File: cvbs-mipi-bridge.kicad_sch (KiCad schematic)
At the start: 114 parts, among them IC1 ADV7282-M, IC2 TLV70018, IC4 SN74AUP1G17DCKR, IC5 SN74AUP1G17DCKR, J1 WE_68715014522, J2 1053131102, J3 KLPX-0848A-2-Y, J4 KLPX-0848A-2-Y, J5 KLPX-0848A-2-Y, J6 KLPX-0848A-2-Y, J7 61300211121, Q1 BSS138APW, Q2 BSS138APW, Q3 BSS138APW, Q4 BSS138APW, Y1 ABM8G-28.63636MHZ-18-D2Y-T

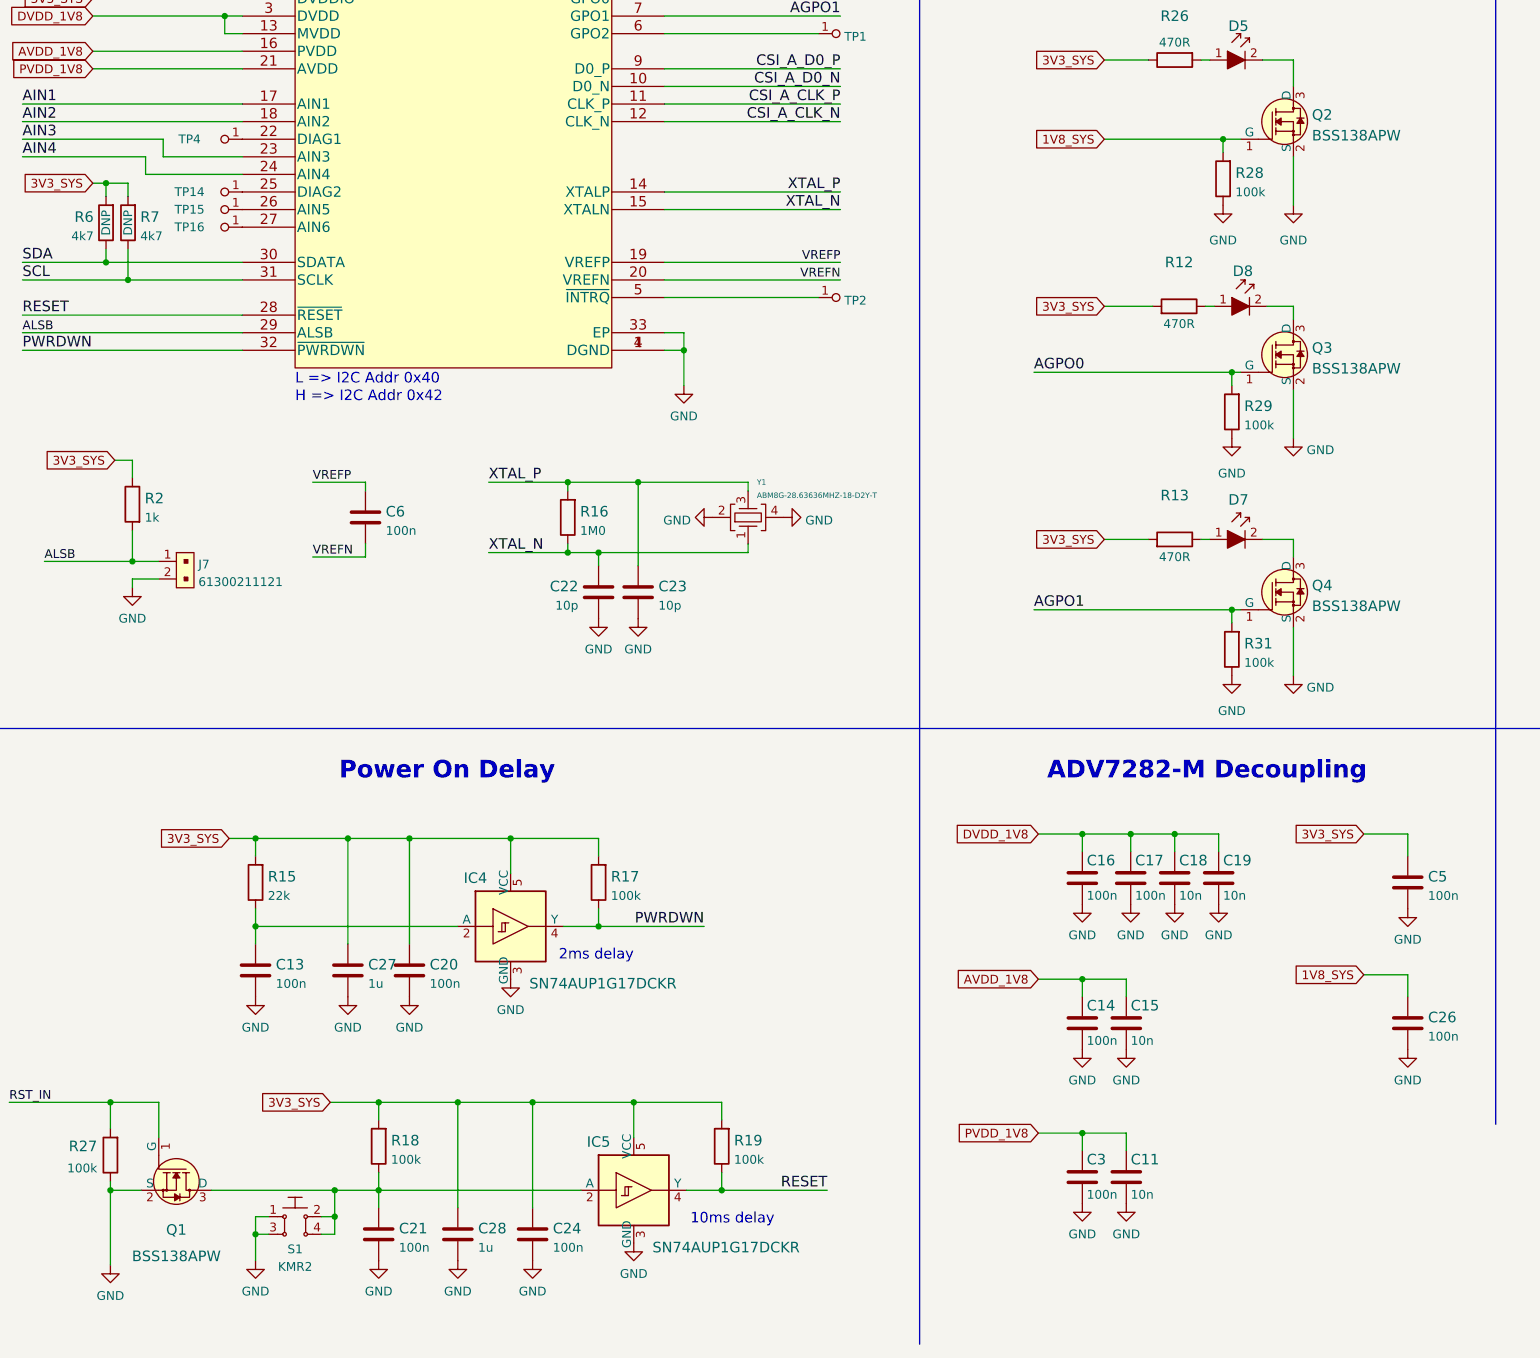
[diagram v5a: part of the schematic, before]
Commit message: Update Q1-Q4 from global library on SCH and PCB
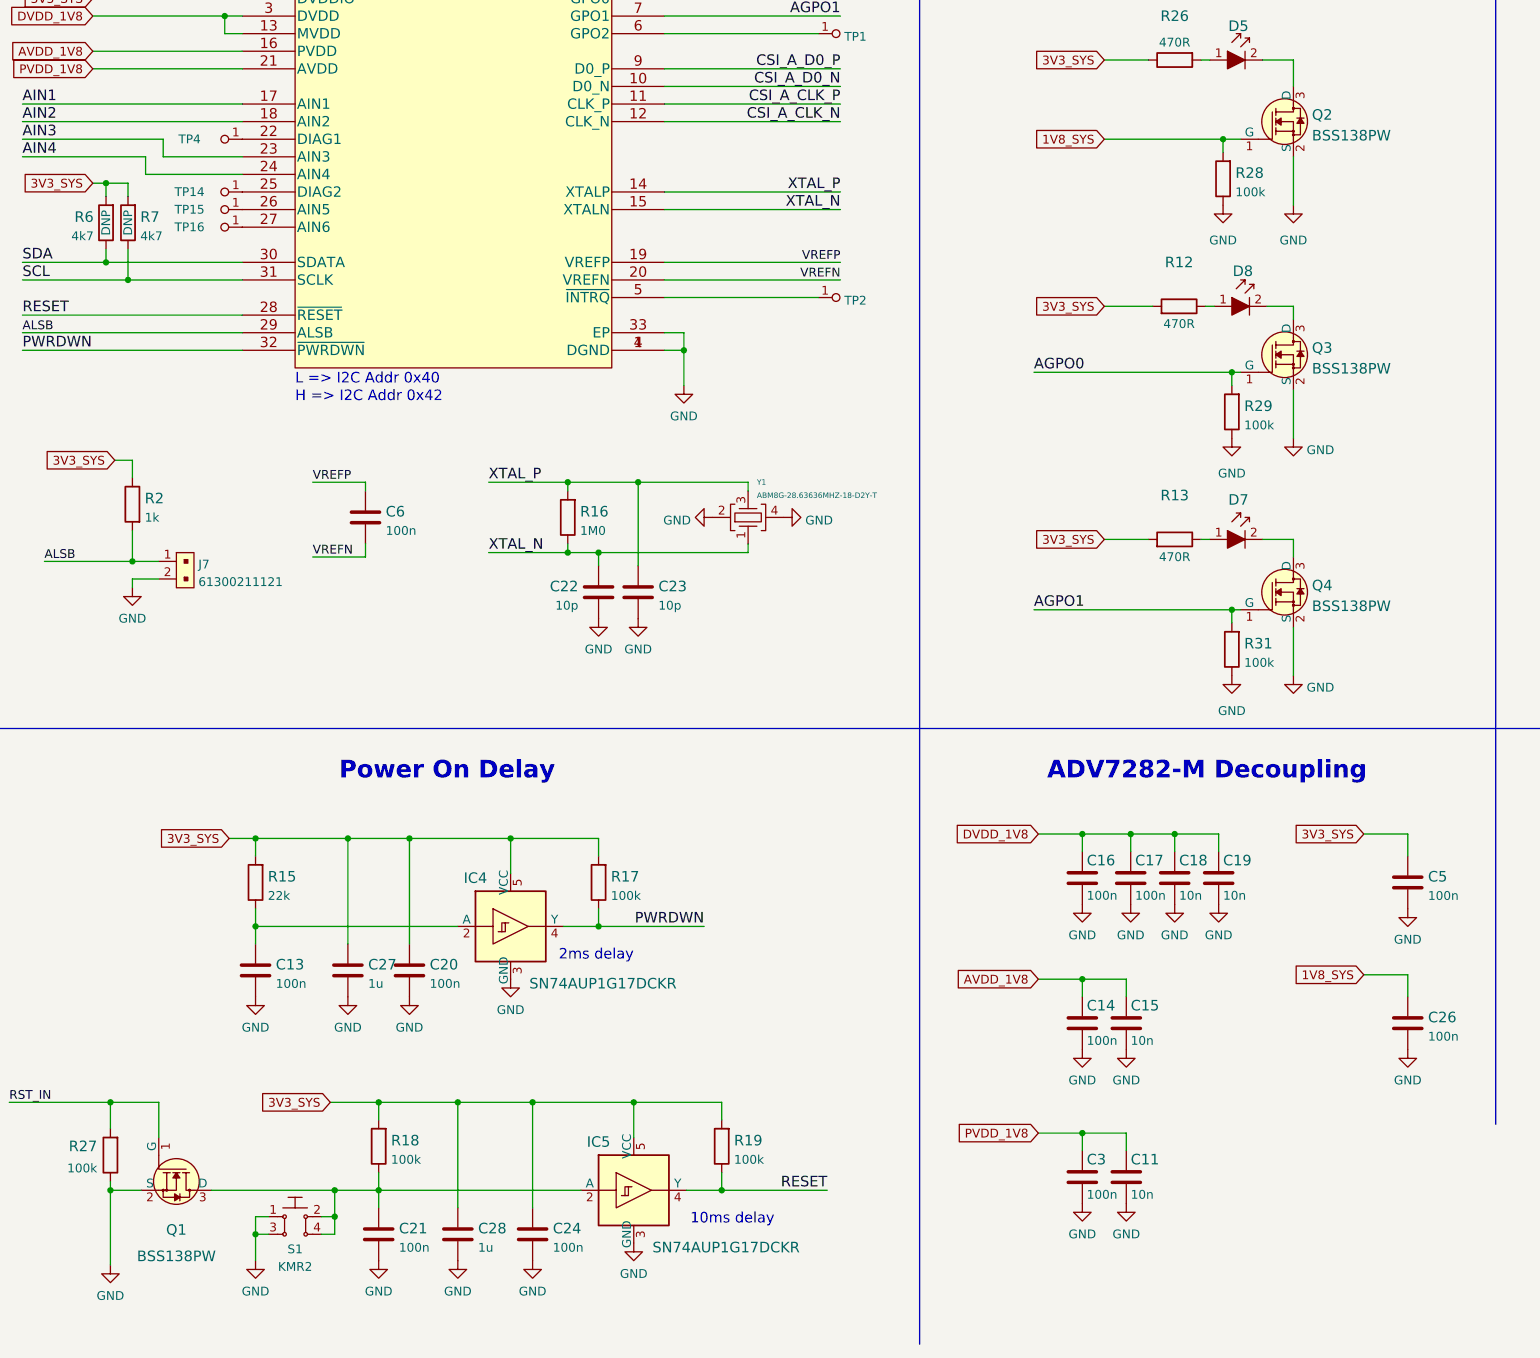
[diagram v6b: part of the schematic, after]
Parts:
- Q1, Q2, Q3, Q4: value BSS138APW -> BSS138PW; footprint cvbs-mipi-bridge-footprints:SC70-3 -> antmicro-footprints:SC70-3; symbol cvbs-mipi-bridge:BSS138APW -> antmicroTransistorsFETsMOSFETsSingle:BSS138PW; Manufacturer ON Semiconductor -> Nexperia
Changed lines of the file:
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@@
     (pin "4")
   )
-  (symbol (lib_id "cvbs-mipi-bridge:BSS138APW") (at 127 262.255 270) (unit 1)
+  (symbol (lib_id "antmicroTransistorsFETsMOSFETsSingle:BSS138PW") (at 127 262.255 270) (unit 1)
     (in_bom yes) (on_board yes) (fields_autoplaced)
     (property "Reference" "Q1" (id 0) (at 127 267.97 90)
       (effects (font (size 1.524 1.524)))
     )
-    (property "Value" "BSS138APW" (id 1) (at 127 271.78 90)
+    (property "Value" "BSS138PW" (id 1) (at 127 271.78 90)
       (effects (font (size 1.524 1.524)))
     )
-    (property "Footprint" "cvbs-mipi-bridge-footprints:SC70-3" (id 2) (at 132.08 267.335 0)
-      (effects (font (size 1.524 1.524)) (justify left) hide)
-    )
-    (property "Datasheet" "" (id 3) (at 134.62 267.335 0)
+    (property "Footprint" "antmicro-footprints:SC70-3" (id 2) (at 132.08 267.335 0)
+      (effects (font (size 1.524 1.524)) (justify left) hide)
+    )
+    (property "Datasheet" "https://assets.nexperia.com/documents/data-sheet/BSS138PW.pdf" (id 3) (at 134.62 267.335 0)
       (effects (font (size 1.524 1.524)) (justify left) hide)
     )
@@
       (effects (font (size 1.524 1.524)) (justify left) hide)
     )
-    (property "Manufacturer" "ON Semiconductor" (id 5) (at 154.94 267.335 0)
+    (property "Manufacturer" "Nexperia" (id 5) (at 154.94 267.335 0)
       (effects (font (size 1.524 1.524)) (justify left) hide)
     )
@@
     (pin "2")
   )
-  (symbol (lib_id "cvbs-mipi-bridge:BSS138APW") (at 288.29 175.895 0) (unit 1)
+  (symbol (lib_id "antmicroTransistorsFETsMOSFETsSingle:BSS138PW") (at 288.29 175.895 0) (unit 1)
     (in_bom yes) (on_board yes)
     (property "Reference" "Q4" (id 0) (at 290.957 174.9188 0)
       (effects (font (size 1.524 1.524)) (justify left))
     )
-    (property "Value" "BSS138APW" (id 1) (at 290.957 177.9122 0)
+    (property "Value" "BSS138PW" (id 1) (at 290.957 177.9122 0)
       (effects (font (size 1.524 1.524)) (justify left))
     )
-    (property "Footprint" "cvbs-mipi-bridge-footprints:SC70-3" (id 2) (at 293.37 170.815 0)
-      (effects (font (size 1.524 1.524)) (justify left) hide)
-    )
-    (property "Datasheet" "" (id 3) (at 293.37 168.275 0)
+    (property "Footprint" "antmicro-footprints:SC70-3" (id 2) (at 293.37 170.815 0)
+      (effects (font (size 1.524 1.524)) (justify left) hide)
+    )
+    (property "Datasheet" "https://assets.nexperia.com/documents/data-sheet/BSS138PW.pdf" (id 3) (at 293.37 168.275 0)
       (effects (font (size 1.524 1.524)) (justify left) hide)
     )
@@
       (effects (font (size 1.524 1.524)) (justify left) hide)
     )
-    (property "Manufacturer" "ON Semiconductor" (id 5) (at 293.37 147.955 0)
+    (property "Manufacturer" "Nexperia" (id 5) (at 293.37 147.955 0)
       (effects (font (size 1.524 1.524)) (justify left) hide)
     )
@@
     (pin "2")
   )
-  (symbol (lib_id "cvbs-mipi-bridge:BSS138APW") (at 288.29 107.95 0) (unit 1)
+  (symbol (lib_id "antmicroTransistorsFETsMOSFETsSingle:BSS138PW") (at 288.29 107.95 0) (unit 1)
     (in_bom yes) (on_board yes)
     (property "Reference" "Q2" (id 0) (at 290.957 106.9738 0)
       (effects (font (size 1.524 1.524)) (justify left))
     )
-    (property "Value" "BSS138APW" (id 1) (at 290.957 109.9672 0)
+    (property "Value" "BSS138PW" (id 1) (at 290.957 109.9672 0)
       (effects (font (size 1.524 1.524)) (justify left))
     )
-    (property "Footprint" "cvbs-mipi-bridge-footprints:SC70-3" (id 2) (at 293.37 102.87 0)
-      (effects (font (size 1.524 1.524)) (justify left) hide)
-    )
-    (property "Datasheet" "" (id 3) (at 293.37 100.33 0)
+    (property "Footprint" "antmicro-footprints:SC70-3" (id 2) (at 293.37 102.87 0)
+      (effects (font (size 1.524 1.524)) (justify left) hide)
+    )
+    (property "Datasheet" "https://assets.nexperia.com/documents/data-sheet/BSS138PW.pdf" (id 3) (at 293.37 100.33 0)
       (effects (font (size 1.524 1.524)) (justify left) hide)
     )
@@
       (effects (font (size 1.524 1.524)) (justify left) hide)
     )
-    (property "Manufacturer" "ON Semiconductor" (id 5) (at 293.37 80.01 0)
+    (property "Manufacturer" "Nexperia" (id 5) (at 293.37 80.01 0)
       (effects (font (size 1.524 1.524)) (justify left) hide)
     )
@@
     (pin "1")
   )
-  (symbol (lib_id "cvbs-mipi-bridge:BSS138APW") (at 288.29 141.605 0) (unit 1)
+  (symbol (lib_id "antmicroTransistorsFETsMOSFETsSingle:BSS138PW") (at 288.29 141.605 0) (unit 1)
     (in_bom yes) (on_board yes)
     (property "Reference" "Q3" (id 0) (at 290.957 140.6288 0)
       (effects (font (size 1.524 1.524)) (justify left))
     )
-    (property "Value" "BSS138APW" (id 1) (at 290.957 143.6222 0)
+    (property "Value" "BSS138PW" (id 1) (at 290.957 143.6222 0)
       (effects (font (size 1.524 1.524)) (justify left))
     )
-    (property "Footprint" "cvbs-mipi-bridge-footprints:SC70-3" (id 2) (at 293.37 136.525 0)
-      (effects (font (size 1.524 1.524)) (justify left) hide)
-    )
-    (property "Datasheet" "" (id 3) (at 293.37 133.985 0)
+    (property "Footprint" "antmicro-footprints:SC70-3" (id 2) (at 293.37 136.525 0)
+      (effects (font (size 1.524 1.524)) (justify left) hide)
+    )
+    (property "Datasheet" "https://assets.nexperia.com/documents/data-sheet/BSS138PW.pdf" (id 3) (at 293.37 133.985 0)
       (effects (font (size 1.524 1.524)) (justify left) hide)
     )
@@
       (effects (font (size 1.524 1.524)) (justify left) hide)
     )
-    (property "Manufacturer" "ON Semiconductor" (id 5) (at 293.37 113.665 0)
+    (property "Manufacturer" "Nexperia" (id 5) (at 293.37 113.665 0)
       (effects (font (size 1.524 1.524)) (justify left) hide)
     )
@@
     )
     (path "/95e1a59b-1a6c-467c-9037-83f08094ade6"
-      (reference "Q1") (unit 1) (value "BSS138APW") (footprint "cvbs-mipi-bridge-footprints:SC70-3")
+      (reference "Q1") (unit 1) (value "BSS138PW") (footprint "antmicro-footprints:SC70-3")
     )
     (path "/f68d1f32-2d93-4f69-b3c5-d0b861598112"
-      (reference "Q2") (unit 1) (value "BSS138APW") (footprint "cvbs-mipi-bridge-footprints:SC70-3")
+      (reference "Q2") (unit 1) (value "BSS138PW") (footprint "antmicro-footprints:SC70-3")
     )
     (path "/fac377af-49d7-4627-96ae-79376b872ab9"
-      (reference "Q3") (unit 1) (value "BSS138APW") (footprint "cvbs-mipi-bridge-footprints:SC70-3")
+      (reference "Q3") (unit 1) (value "BSS138PW") (footprint "antmicro-footprints:SC70-3")
     )
     (path "/aad57a2e-9eca-4168-bc4f-4b035b4e6956"
-      (reference "Q4") (unit 1) (value "BSS138APW") (footprint "cvbs-mipi-bridge-footprints:SC70-3")
+      (reference "Q4") (unit 1) (value "BSS138PW") (footprint "antmicro-footprints:SC70-3")
     )
     (path "/44b415ce-6f62-45ef-b8e2-efa97d049c0e"

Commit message: Increase revision number to 1.0.1 - update title blocks & PCB marking
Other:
- company: (none) -> Antmicro Ltd.
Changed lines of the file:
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@@
   (title_block
     (title "CVBS-MIPI Bridge")
-    (date "2022-09-29")
-    (rev "1.0.0")
+    (date "2022-11-04")
+    (rev "1.0.1")
+    (company "Antmicro Ltd.")
     (comment 1 "www.antmicro.com")
-    (comment 2 "Antmicro Ltd.")
   )
   (junction (at 69.088 115.57) (diameter 0) (color 0 0 0 0)

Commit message: SCH: Change selected Power On Delay elements' footprints to thermal-relief variants
Thermal reliefs added to: R27, C13, C20, C21, C24, C27, C28
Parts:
- C13, C20, C21, C24, C27, C28: footprint cvbs-mipi-bridge-footprints:0402-cap -> cvbs-mipi-bridge-footprints:0402-cap_ThermalReliefs_ZoneSizeSettings
- R27: footprint cvbs-mipi-bridge-footprints:0402-res -> cvbs-mipi-bridge-footprints:0402-res_ThermalReliefs_ZoneSizeSettings
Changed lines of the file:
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@@
       (effects (font (size 1.524 1.524)) hide)
     )
-    (property "Footprint" "cvbs-mipi-bridge-footprints:0402-cap" (id 2) (at 183.515 263.525 0)
+    (property "Footprint" "cvbs-mipi-bridge-footprints:0402-cap_ThermalReliefs_ZoneSizeSettings" (id 2) (at 183.515 263.525 0)
       (effects (font (size 1.524 1.524)) (justify left) hide)
     )
@@
       (effects (font (size 1.524 1.524)) hide)
     )
-    (property "Footprint" "cvbs-mipi-bridge-footprints:0402-cap" (id 2) (at 143.51 225.425 0)
+    (property "Footprint" "cvbs-mipi-bridge-footprints:0402-cap_ThermalReliefs_ZoneSizeSettings" (id 2) (at 143.51 225.425 0)
       (effects (font (size 1.524 1.524)) (justify left) hide)
     )
@@
       (effects (font (size 1.524 1.524)) hide)
     )
-    (property "Footprint" "cvbs-mipi-bridge-footprints:0402-cap" (id 2) (at 161.29 263.525 0)
+    (property "Footprint" "cvbs-mipi-bridge-footprints:0402-cap_ThermalReliefs_ZoneSizeSettings" (id 2) (at 161.29 263.525 0)
       (effects (font (size 1.524 1.524)) (justify left) hide)
     )
@@
       (effects (font (size 1.524 1.524)) hide)
     )
-    (property "Footprint" "cvbs-mipi-bridge-footprints:0402-cap" (id 2) (at 172.72 263.525 0)
+    (property "Footprint" "cvbs-mipi-bridge-footprints:0402-cap_ThermalReliefs_ZoneSizeSettings" (id 2) (at 172.72 263.525 0)
       (effects (font (size 1.524 1.524)) (justify left) hide)
     )
@@
       (effects (font (size 1.524 1.524)) hide)
     )
-    (property "Footprint" "cvbs-mipi-bridge-footprints:0402-cap" (id 2) (at 156.845 225.425 0)
+    (property "Footprint" "cvbs-mipi-bridge-footprints:0402-cap_ThermalReliefs_ZoneSizeSettings" (id 2) (at 156.845 225.425 0)
       (effects (font (size 1.524 1.524)) (justify left) hide)
     )
@@
       (effects (font (size 1.524 1.524)) hide)
     )
-    (property "Footprint" "cvbs-mipi-bridge-footprints:0402-cap" (id 2) (at 165.735 225.425 0)
+    (property "Footprint" "cvbs-mipi-bridge-footprints:0402-cap_ThermalReliefs_ZoneSizeSettings" (id 2) (at 165.735 225.425 0)
       (effects (font (size 1.524 1.524)) (justify left) hide)
     )
@@
       (effects (font (size 1.524 1.524)) hide)
     )
-    (property "Footprint" "cvbs-mipi-bridge-footprints:0402-res" (id 2) (at 112.395 252.095 0)
+    (property "Footprint" "cvbs-mipi-bridge-footprints:0402-res_ThermalReliefs_ZoneSizeSettings" (id 2) (at 112.395 252.095 0)
       (effects (font (size 1.524 1.524)) (justify left) hide)
     )
@@
     )
     (path "/1bee2d5b-6bc8-4cce-a6e3-1f3bf9745bb9"
-      (reference "C13") (unit 1) (value "C_100n_0402") (footprint "cvbs-mipi-bridge-footprints:0402-cap")
+      (reference "C13") (unit 1) (value "C_100n_0402") (footprint "cvbs-mipi-bridge-footprints:0402-cap_ThermalReliefs_ZoneSizeSettings")
     )
     (path "/a6cf3c89-c358-4fe5-8c48-55a885e26635"
@@
     )
     (path "/d9a4ccc3-9031-42be-9255-f7e52bdbb0e2"
-      (reference "C20") (unit 1) (value "C_100n_0402") (footprint "cvbs-mipi-bridge-footprints:0402-cap")
+      (reference "C20") (unit 1) (value "C_100n_0402") (footprint "cvbs-mipi-bridge-footprints:0402-cap_ThermalReliefs_ZoneSizeSettings")
     )
     (path "/3fc12d68-fcb6-48b6-8065-f1ad670bea04"
-      (reference "C21") (unit 1) (value "C_100n_0402") (footprint "cvbs-mipi-bridge-footprints:0402-cap")
+      (reference "C21") (unit 1) (value "C_100n_0402") (footprint "cvbs-mipi-bridge-footprints:0402-cap_ThermalReliefs_ZoneSizeSettings")
     )
     (path "/b27a027d-42b4-40c4-8859-9d82b6860bf7"
@@
     )
     (path "/09a3076f-3165-4f6a-9373-edde30364cee"
-      (reference "C24") (unit 1) (value "C_100n_0402") (footprint "cvbs-mipi-bridge-footprints:0402-cap")
+      (reference "C24") (unit 1) (value "C_100n_0402") (footprint "cvbs-mipi-bridge-footprints:0402-cap_ThermalReliefs_ZoneSizeSettings")
     )
     (path "/a1f98d0c-4255-4671-b54f-e111015a429f"
@@
     )
     (path "/a9ff00fd-c74f-4da8-8c76-a9035957e9cf"
-      (reference "C27") (unit 1) (value "C_1u_0402") (footprint "cvbs-mipi-bridge-footprints:0402-cap")
+      (reference "C27") (unit 1) (value "C_1u_0402") (footprint "cvbs-mipi-bridge-footprints:0402-cap_ThermalReliefs_ZoneSizeSettings")
     )
     (path "/a906aa26-a996-49f0-ad55-0360891fb415"
-      (reference "C28") (unit 1) (value "C_1u_0402") (footprint "cvbs-mipi-bridge-footprints:0402-cap")
+      (reference "C28") (unit 1) (value "C_1u_0402") (footprint "cvbs-mipi-bridge-footprints:0402-cap_ThermalReliefs_ZoneSizeSettings")
     )
     (path "/c13c5692-c189-4d8d-8200-667b0d08dcd1"
@@
     )
     (path "/f25932ef-461a-431a-b3df-e3ea8576a101"
-      (reference "R27") (unit 1) (value "R_100k_0402") (footprint "cvbs-mipi-bridge-footprints:0402-res")
+      (reference "R27") (unit 1) (value "R_100k_0402") (footprint "cvbs-mipi-bridge-footprints:0402-res_ThermalReliefs_ZoneSizeSettings")
     )
     (path "/adf25e91-eb6c-4a50-a77b-bc415cbc1747"
